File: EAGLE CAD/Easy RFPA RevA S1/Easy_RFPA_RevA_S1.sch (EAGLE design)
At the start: 197 parts, among them J101 COAX112640BNC_EDGE, J102 COAX112640BNC_EDGE, J301 COAX112640BNC_EDGE, J302 COAX112640BNC_EDGE, J401 HDR_2X1282836-1282836-1, J402 KK_PCFAN, Q101 IRF520N, Q102 IRF630, Q201 IRF630, Q202 IRF630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

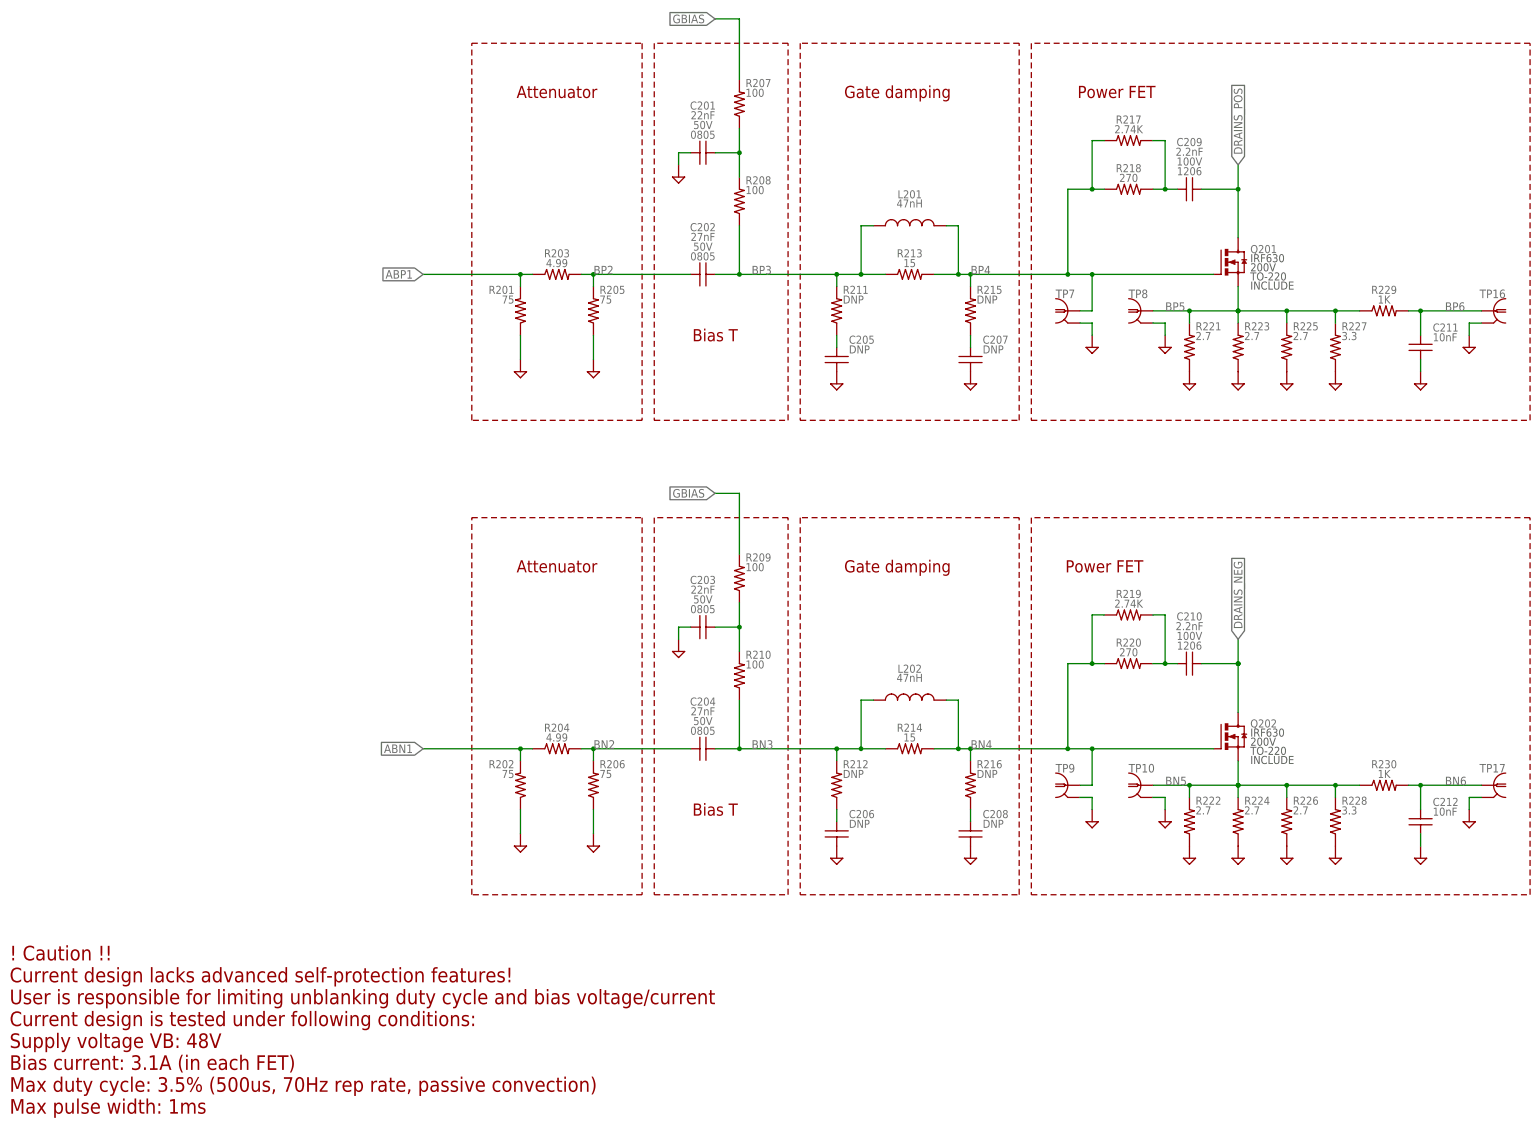
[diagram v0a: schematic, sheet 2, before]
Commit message: S1 component values
Change component values for S1
Also fix a couple in S2
Export BOM and pdf for S1
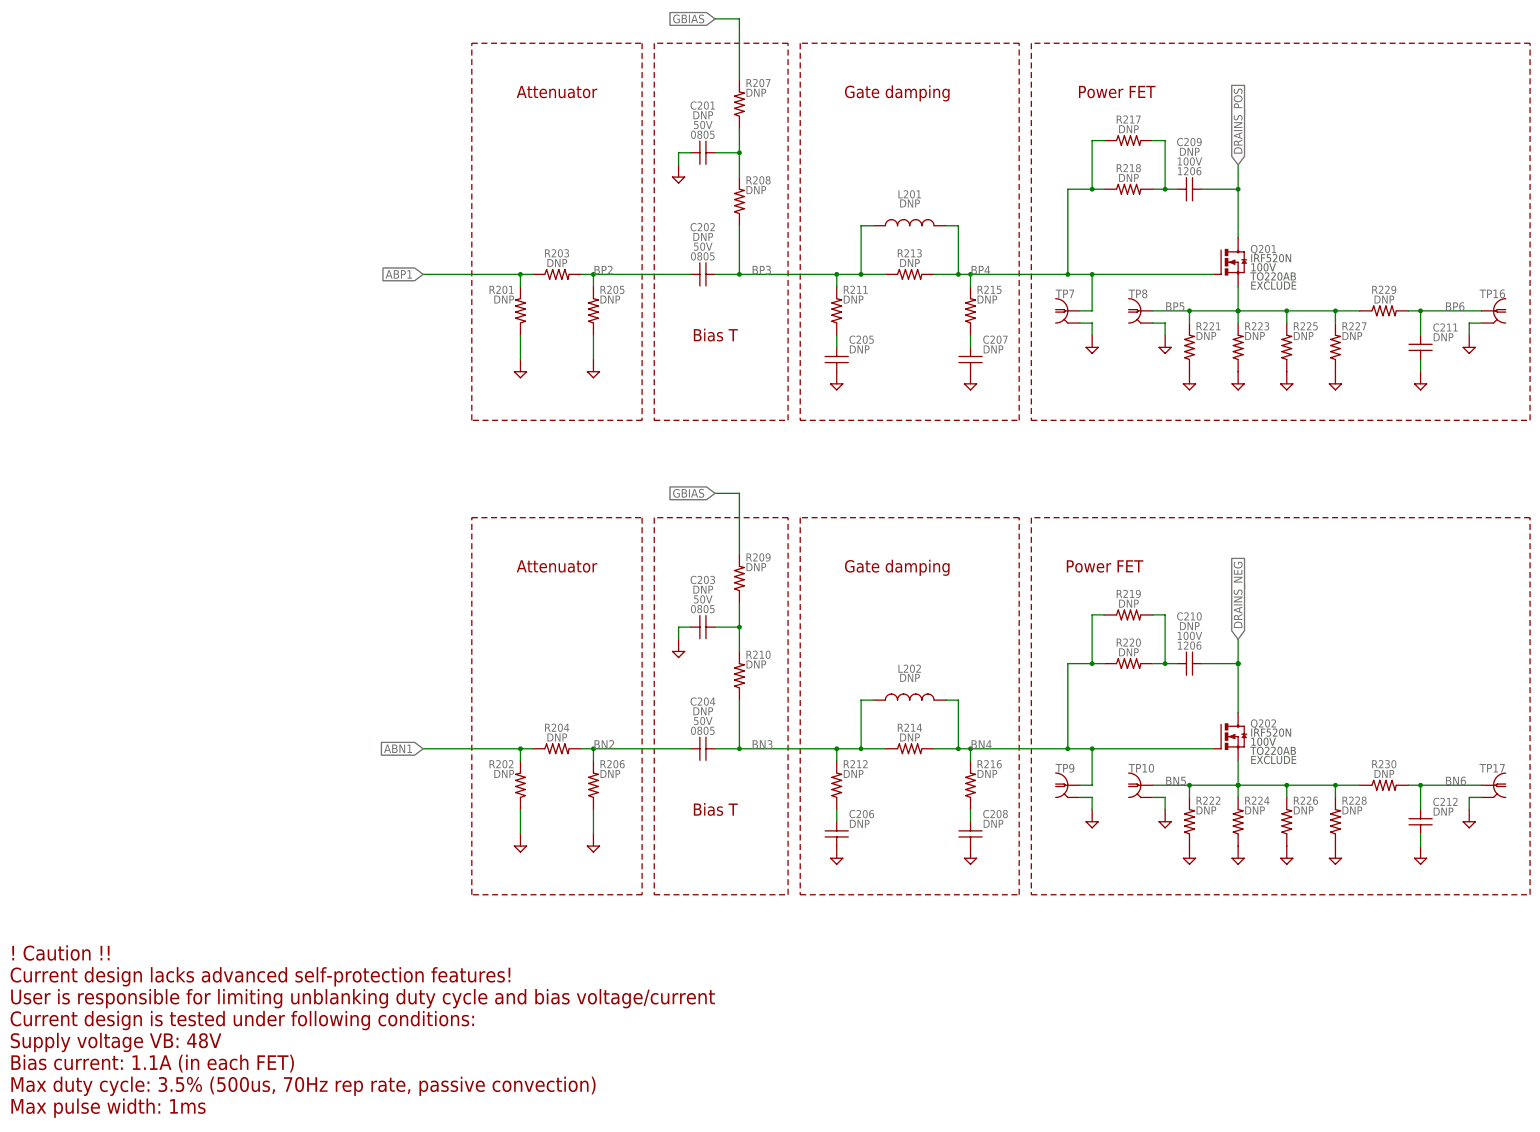
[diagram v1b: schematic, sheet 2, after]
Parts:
- C101, C118: value DNP -> 0.1uF; BOM EXCLUDE -> (none)
- C103, C120: value 3nF -> DNP; BOM (none) -> EXCLUDE
- C105, C107: value 27nF -> 12nF
- C112, C113: value 22nF -> 2.2nF
- C201, C203: value 22nF -> DNP; BOM (none) -> EXCLUDE
- C202, C204: value 27nF -> DNP; BOM (none) -> EXCLUDE
- C209, C210: value 2.2nF -> DNP; BOM (none) -> EXCLUDE
- C211, C212: value 10nF -> DNP; BOM (none) -> EXCLUDE
- L103, L104: value 3.3uH -> 22uH; device MDT_L:LL-3.3U-FERRITE-20%-12.5X12.5MM-10.5A -> MDT_L:LL-22U-FERRITE-20%-12.5X12.5MM-4A
- L201, L202: value 47nH -> DNP; BOM (none) -> EXCLUDE
- Q101: device MDT_TRANS:MOSFET_NIRF630TO-220-VERT -> MDT_TRANS:MOSFET_NIRF520NTO-220-VERT
- Q102: value IRF630 -> IRF520N; device MDT_TRANS:MOSFET_NIRF630TO-220-VERT -> MDT_TRANS:MOSFET_NIRF520NTO-220-VERT
- Q201, Q202: device MDT_TRANS:MOSFET_NIRF630TO-220-VERT -> MDT_TRANS:MOSFET_NIRF520NTO-220-VERT; BOM (none) -> EXCLUDE
- R102, R103, R106, R107: value 75 -> 220
- R122, R123, R124, R125: value 2.7 -> 6.8
- R126, R127: value 2.7 -> 8.2
- R128, R129: value 3.3 -> 8.2
- R201, R202, R205, R206: value 75 -> DNP; BOM (none) -> EXCLUDE
- R203, R204: value 4.99 -> DNP; BOM (none) -> EXCLUDE
- R207, R208, R209, R210: value 100 -> DNP; BOM (none) -> EXCLUDE
- R213, R214: value 15 -> DNP; BOM (none) -> EXCLUDE
- R217, R219: value 2.74K -> DNP; BOM (none) -> EXCLUDE
- R218, R220: value 270 -> DNP; BOM (none) -> EXCLUDE
- R221, R222, R223, R224, R225, R226: value 2.7 -> DNP; BOM (none) -> EXCLUDE
- R227, R228: value 3.3 -> DNP; BOM (none) -> EXCLUDE
- R229, R230: value 1K -> DNP; BOM (none) -> EXCLUDE
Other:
- note added: "! Caution !! Current design lacks advanced self-protection features! User is responsible for limiting unblanking duty cycle and bias voltage/current Current design is tested under following conditions: Supply voltage VB: 48V Bias current: 1.1A (in each FET) Max duty cycle: 3.5% (500us, 70Hz rep rate, passive convection) Max pulse width: 1ms"
- note removed: "! Caution !! Current design lacks advanced self-protection features! User is responsible for limiting unblanking duty cycle and bias voltage/current Current design is tested under following conditions: Supply voltage VB: 48V Bias current: 3.1A (in each FET) Max duty cycle: 3.5% (500us, 70Hz rep rate, passive convection) Max pulse width: 1ms"

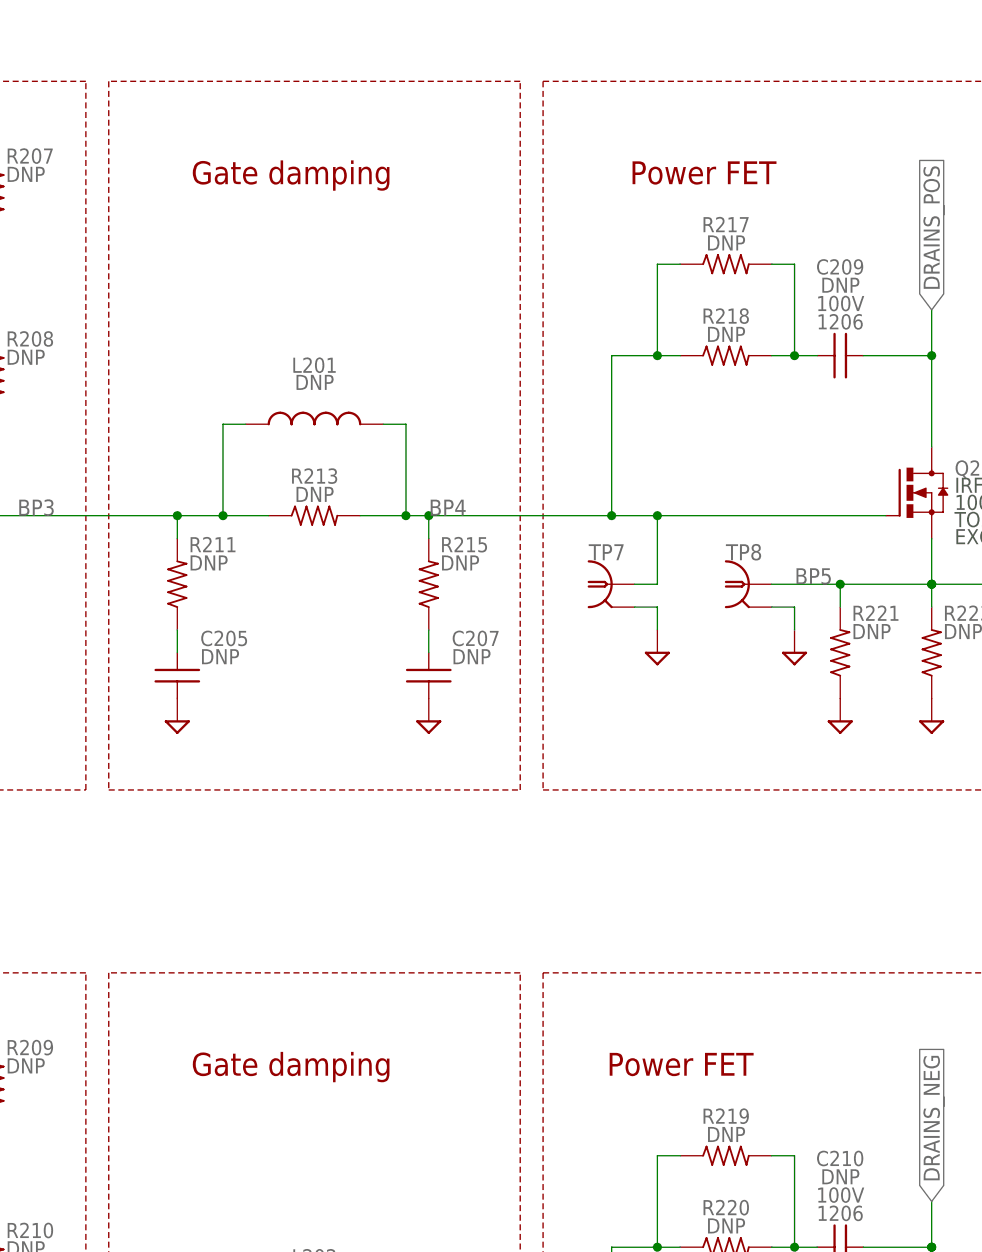
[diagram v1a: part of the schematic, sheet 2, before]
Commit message: Copy revA S2 to new revB S2
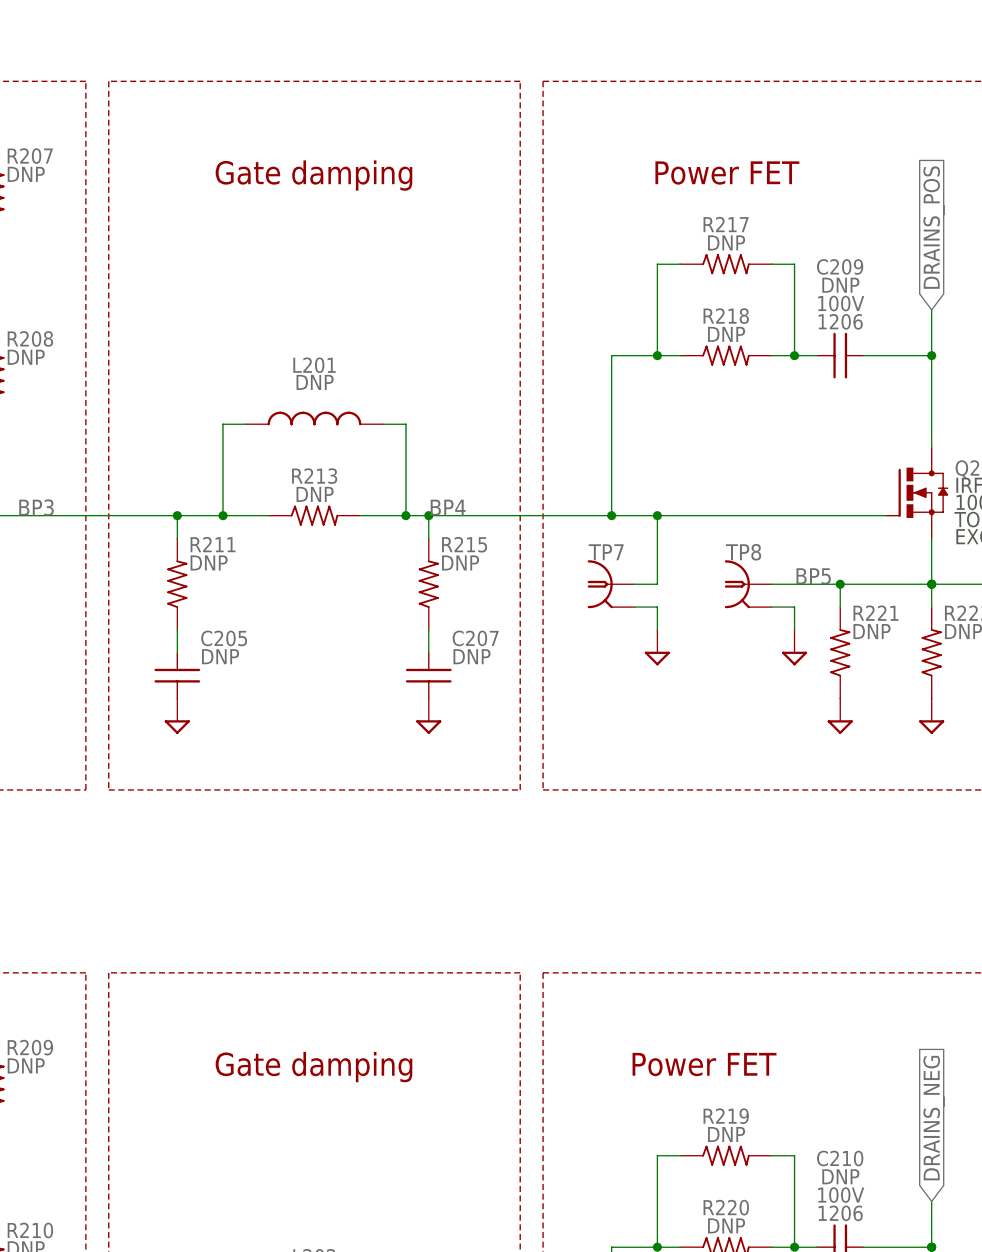
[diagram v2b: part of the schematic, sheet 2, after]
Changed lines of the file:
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@@
 <text x="154.94" y="167.64" size="2.54" layer="94" align="center">Bias T</text>
 <text x="154.94" y="68.58" size="2.54" layer="94" align="center">Bias T</text>
-<text x="193.04" y="218.44" size="2.54" layer="94" align="center">Gate damping</text>
-<text x="193.04" y="119.38" size="2.54" layer="94" align="center">Gate damping</text>
-<text x="238.76" y="218.44" size="2.54" layer="94" align="center">Power FET</text>
-<text x="236.22" y="119.38" size="2.54" layer="94" align="center">Power FET</text>
+<text x="195.58" y="218.44" size="2.54" layer="94" align="center">Gate damping</text>
+<text x="195.58" y="119.38" size="2.54" layer="94" align="center">Gate damping</text>
+<text x="241.3" y="218.44" size="2.54" layer="94" align="center">Power FET</text>
+<text x="238.76" y="119.38" size="2.54" layer="94" align="center">Power FET</text>
 <text x="7.62" y="5.08" size="3.048" layer="94">! Caution !!
 Current design lacks advanced self-protection features!

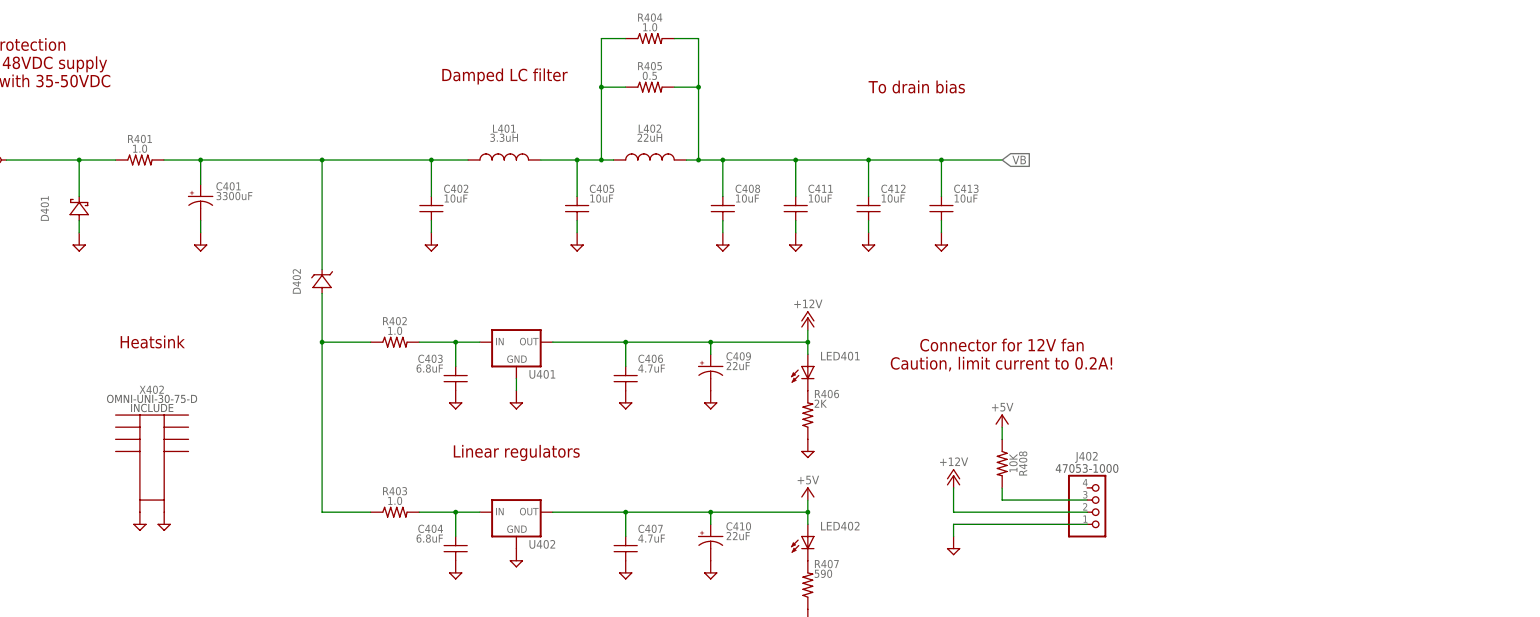
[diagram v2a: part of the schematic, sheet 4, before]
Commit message: Copy the pads and clips to revA S1 and S2
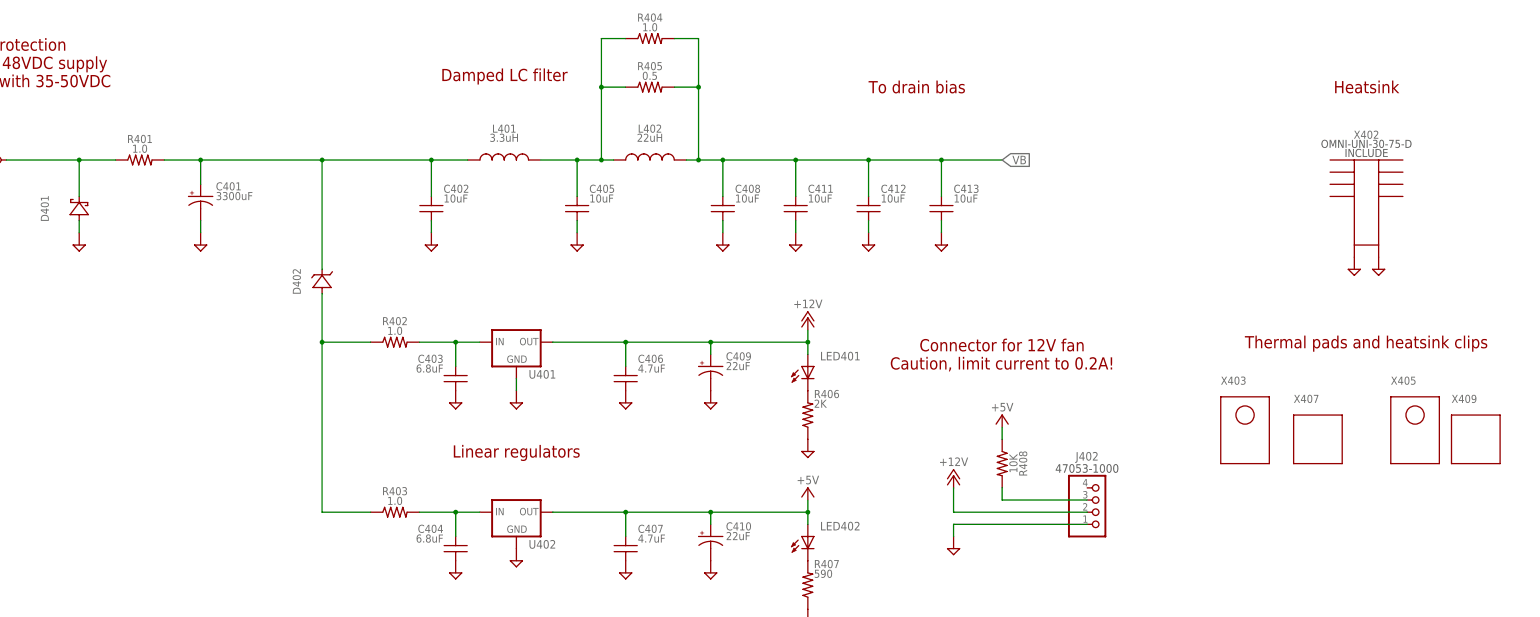
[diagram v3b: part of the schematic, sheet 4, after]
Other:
- note added: "Thermal pads and heatsink clips"
- moved on the sheet: X402
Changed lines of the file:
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@@
 </part>
 <part name="J401" library="MDT_CON" deviceset="HDR_2X1" device="282836-1" technology="282836-1"/>
+<part name="X403" library="MDT_HEATSINK" deviceset="THERMALPAD_TO220" device="" technology="DC0011/15-TI900-0.12-0"/>
+<part name="X405" library="MDT_HEATSINK" deviceset="THERMALPAD_TO220" device="" technology="DC0011/15-TI900-0.12-0"/>
+<part name="X407" library="MDT_HEATSINK" deviceset="HEATSINK_CLIP" device="" technology="OMNI-220C"/>
+<part name="X409" library="MDT_HEATSINK" deviceset="HEATSINK_CLIP" device="" technology="OMNI-220C"/>
 </parts>
 <sheets>
@@
 <plain>
 <text x="73.66" y="137.16" size="2.54" layer="94" align="center">Mounting holes</text>
-<text x="121.92" y="137.16" size="2.54" layer="94" align="center">Heatsink</text>
+<text x="375.92" y="190.5" size="2.54" layer="94" align="center">Heatsink</text>
 <text x="91.44" y="195.58" size="2.54" layer="94" align="center">Input protection
 Intended for 48VDC supply
@@
 Max duty cycle: 3.5% (500us, 70Hz rep rate, passive convection)
 Max pulse width: 1ms</text>
+<text x="375.92" y="137.16" size="2.54" layer="94" align="center">Thermal pads and heatsink clips</text>
 </plain>
 <instances>
@@
 <instance part="SUPPLY410" gate="GND" x="220.98" y="124.46" smashed="yes"/>
 <instance part="SUPPLY411" gate="GND" x="220.98" y="88.9" smashed="yes"/>
-<instance part="SUPPLY421" gate="GND" x="119.38" y="99.06" smashed="yes"/>
-<instance part="SUPPLY422" gate="GND" x="124.46" y="99.06" smashed="yes"/>
-<instance part="X402" gate="G$1" x="121.92" y="104.14"/>
+<instance part="SUPPLY421" gate="GND" x="373.38" y="152.4" smashed="yes"/>
+<instance part="SUPPLY422" gate="GND" x="378.46" y="152.4" smashed="yes"/>
+<instance part="X402" gate="G$1" x="375.92" y="157.48"/>
 <instance part="F401" gate="G$1" x="83.82" y="175.26" smashed="yes">
 <attribute name="NAME" x="83.82" y="180.34" size="1.778" layer="95" align="bottom-center"/>
@@
 <instance part="SUPPLY413" gate="GND" x="238.76" y="124.46" smashed="yes"/>
 <instance part="J401" gate="G$1" x="55.88" y="172.72" rot="MR0"/>
+<instance part="X403" gate="G$1" x="350.52" y="121.92"/>
+<instance part="X405" gate="G$1" x="386.08" y="121.92"/>
+<instance part="X407" gate="G$1" x="365.76" y="116.84"/>
+<instance part="X409" gate="G$1" x="398.78" y="116.84"/>
 </instances>
 <busses>
